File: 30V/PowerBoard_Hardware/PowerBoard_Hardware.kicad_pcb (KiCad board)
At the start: 2 copper layers, 145.4 x 114.3 mm, 114 parts, among them Q1 Q_NMOS_DGS, Q2 Q_NMOS_DGS, Q3 Q_NMOS_DGS, Q4 Q_NMOS_DGS, Q5 Q_NMOS_DGS, Q6 Q_NMOS_DGS, Q7 Q_NMOS_DGS, U1 LT1910, U10 LT1910, U11 LT1910, U12 ACS722xLCTR-40AU, U13 ACS722xLCTR-40AU, U14 ACS722xLCTR-40AU, U15 OKI, U16 OKI, U2 LT1910, U3 LT1910, U4 LT1910, U5 ACS722xLCTR-40AU, U6 ACS722xLCTR-40AU, U7 ACS722xLCTR-40AU, U8 ACS722xLCTR-40AU, U9 LT1910

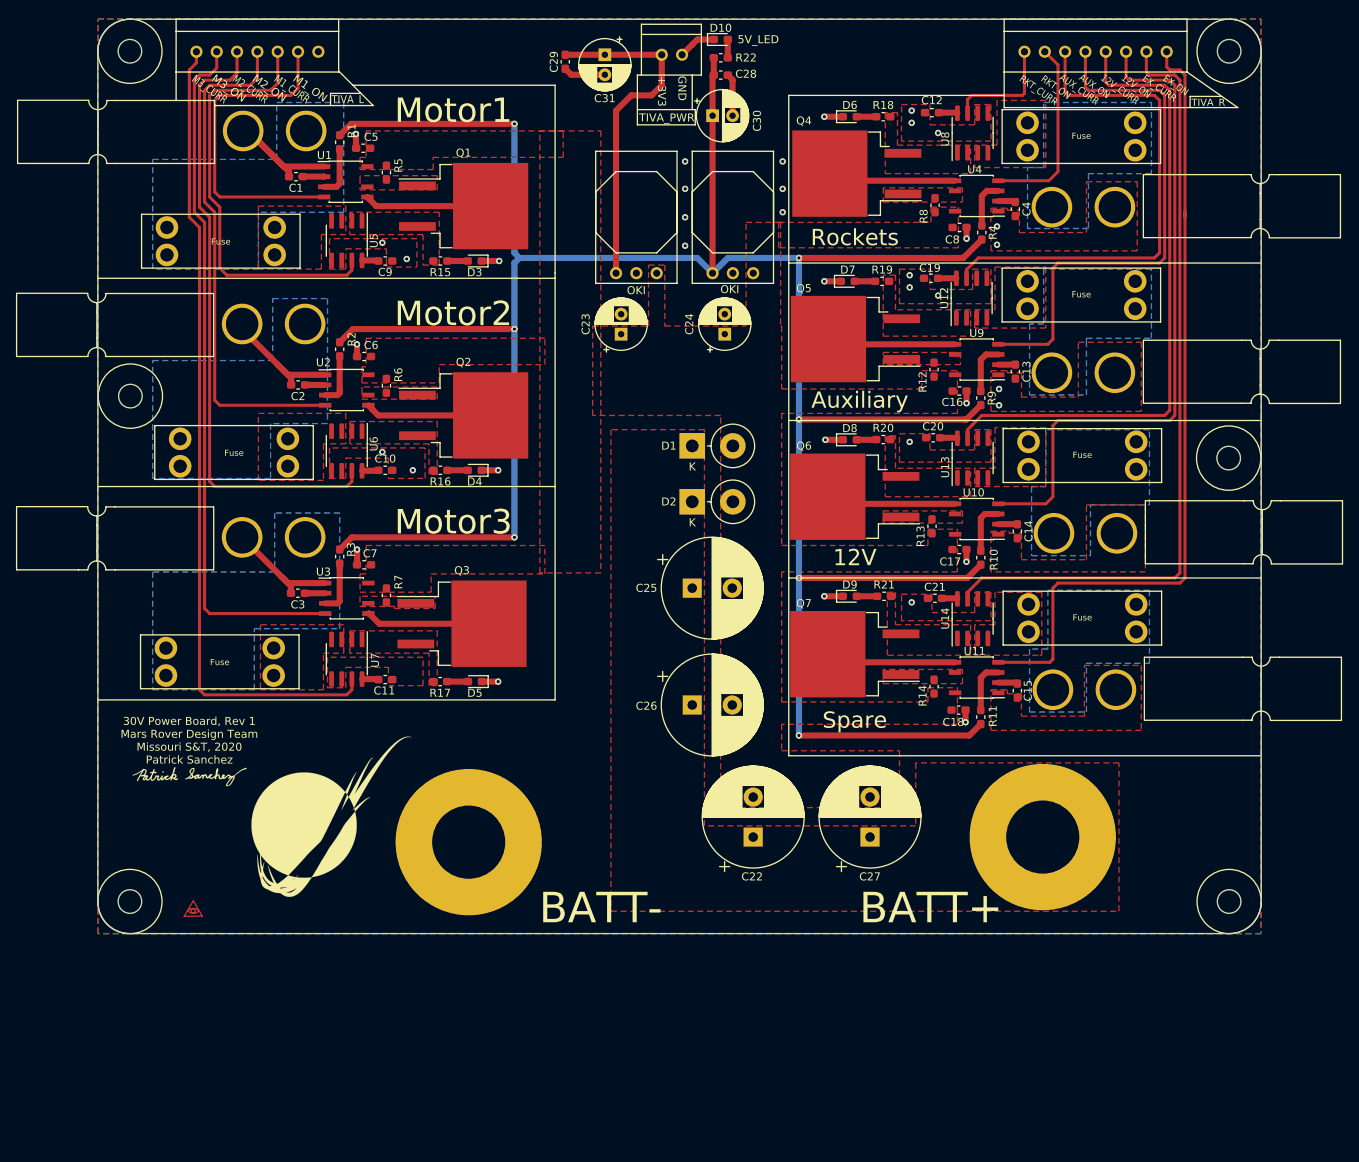
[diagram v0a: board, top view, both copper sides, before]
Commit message: Overwriting for proper file structure
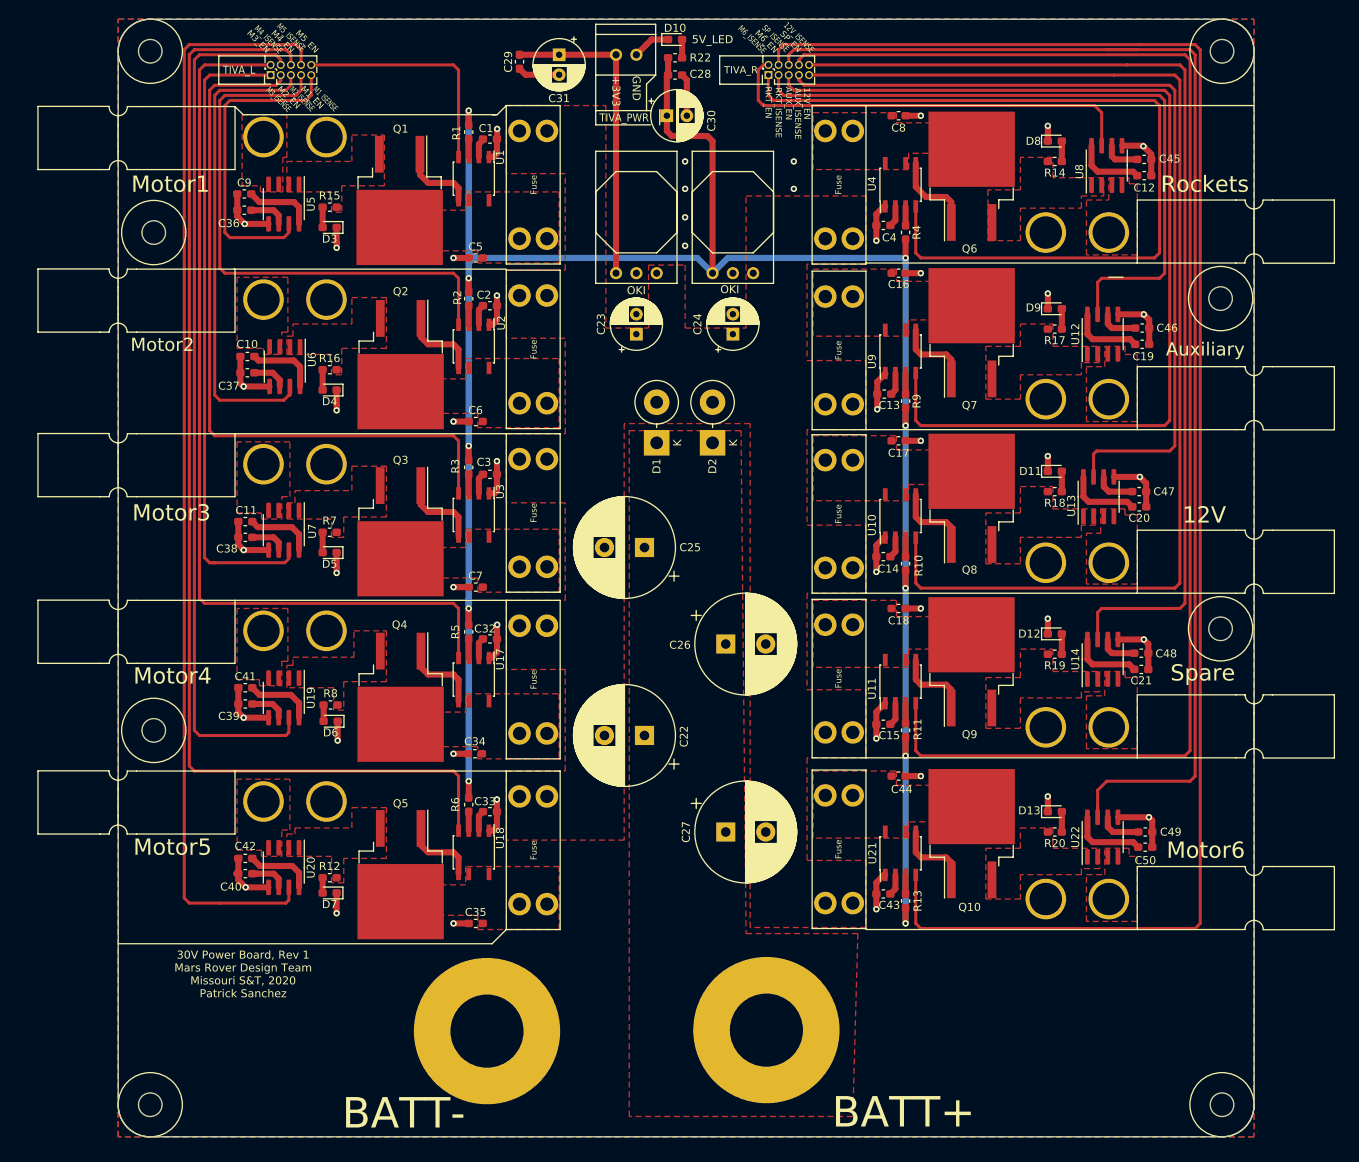
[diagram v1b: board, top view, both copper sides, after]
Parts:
- removed G***: LOGO, MRDT_Silkscreens:2_Nothing_3mm_Cu
- removed G***: LOGO, MRDT_Silkscreens:0_MRDT_Logo_20mm
- removed G***: LOGO, MRDT_Silkscreens:z_sig_Patrick_Sanchez_15mmx5mm
- removed R21: 1.5k, Resistor_SMD:R_0603_1608Metric_Pad1.05x0.95mm_HandSolder
- removed the REF** at (98.0, 77.6)
- removed the REF** at (235.3, 85.3)
- removed the REF** at (94.0, 144.8)
- removed the REF** at (239.4, 144.8)
- removed the REF** at (239.4, 30.5)
- removed the REF** at (94.0, 30.5)
- added C32: 0.1 uF, Capacitor_SMD:C_0603_1608Metric_Pad1.05x0.95mm_HandSolder, F.Cu at (143.0, 108.0)
- added C33: 0.1 uF, Capacitor_SMD:C_0603_1608Metric_Pad1.05x0.95mm_HandSolder, F.Cu at (143.0, 129.5)
- added C34: 10uF 50V, Capacitor_SMD:C_0603_1608Metric_Pad1.05x0.95mm_HandSolder, F.Cu at (141.1, 122.3)
- added C35: 10uF 50V, Capacitor_SMD:C_0603_1608Metric_Pad1.05x0.95mm_HandSolder, F.Cu at (141.2, 143.5)
- added C36: 1nF, Capacitor_SMD:C_0603_1608Metric_Pad1.05x0.95mm_HandSolder, F.Cu at (112.3, 54.4)
- added C37: 1nF, Capacitor_SMD:C_0603_1608Metric_Pad1.05x0.95mm_HandSolder, F.Cu at (112.7, 74.7)
- added C38: 1nF, Capacitor_SMD:C_0603_1608Metric_Pad1.05x0.95mm_HandSolder, F.Cu at (112.4, 95.2)
- added C39: 1nF, Capacitor_SMD:C_0603_1608Metric_Pad1.05x0.95mm_HandSolder, F.Cu at (112.4, 116.1)
- added C40: 1nF, Capacitor_SMD:C_0603_1608Metric_Pad1.05x0.95mm_HandSolder, F.Cu at (112.4, 137.3)
- added C41: 0.1 uF, Capacitor_SMD:C_0603_1608Metric_Pad1.05x0.95mm_HandSolder, F.Cu at (112.4, 114.0)
- added C42: 0.1 uF, Capacitor_SMD:C_0603_1608Metric_Pad1.05x0.95mm_HandSolder, F.Cu at (112.4, 135.4)
- added C43: 0.1 uF, Capacitor_SMD:C_0603_1608Metric_Pad1.05x0.95mm_HandSolder, F.Cu at (192.2, 139.8)
- added C44: 10uF 50V, Capacitor_SMD:C_0603_1608Metric_Pad1.05x0.95mm_HandSolder, F.Cu at (194.1, 125.1)
- added C45: 1nF, Capacitor_SMD:C_0603_1608Metric_Pad1.05x0.95mm_HandSolder, F.Cu at (224.8, 48.0)
- added C46: 1nF, Capacitor_SMD:C_0603_1608Metric_Pad1.05x0.95mm_HandSolder, F.Cu at (224.5, 69.1)
- added C47: 1nF, Capacitor_SMD:C_0603_1608Metric_Pad1.05x0.95mm_HandSolder, F.Cu at (224.1, 89.5)
- added C48: 1nF, Capacitor_SMD:C_0603_1608Metric_Pad1.05x0.95mm_HandSolder, F.Cu at (224.4, 109.7)
- added C49: 1nF, Capacitor_SMD:C_0603_1608Metric_Pad1.05x0.95mm_HandSolder, F.Cu at (224.9, 132.1)
- added C50: 0.1 uF, Capacitor_SMD:C_0603_1608Metric_Pad1.05x0.95mm_HandSolder, F.Cu at (224.9, 134.0)
- added Conn10: AndersonPP, MRDT_Connectors:Anderson_2_Horizontal_Stacked, F.Cu at (220.3, 140.5)
- added Conn6: AndersonPP, MRDT_Connectors:Anderson_2_Horizontal_Stacked, F.Cu at (220.3, 57.1)
- added Conn7: AndersonPP, MRDT_Connectors:Anderson_2_Horizontal_Stacked, F.Cu at (220.3, 78.0)
- added D11: GRN, LED_SMD:LED_0603_1608Metric_Pad1.05x0.95mm_HandSolder, F.Cu at (213.6, 87.0)
- added D12: ORG, LED_SMD:LED_0603_1608Metric_Pad1.05x0.95mm_HandSolder, F.Cu at (213.6, 107.3)
- added D13: ORG, LED_SMD:LED_0603_1608Metric_Pad1.05x0.95mm_HandSolder, F.Cu at (213.6, 129.5)
- added F10: Fuse, MRDT_Passives:ATC_Fuse_Block, F.Cu at (190.0, 144.1)
- added F8: Fuse, MRDT_Passives:ATC_Fuse_Block, F.Cu at (145.0, 103.1)
- added F9: Fuse, MRDT_Passives:ATC_Fuse_Block, F.Cu at (145.0, 124.5)
- added Q10: Q_NMOS_GDS, Package_TO_SOT_SMD:TO-263-2, F.Cu at (203.2, 132.3)
- added Q8: Q_NMOS_GDS, Package_TO_SOT_SMD:TO-263-2, F.Cu at (203.2, 90.4)
- added Q9: Q_NMOS_GDS, Package_TO_SOT_SMD:TO-263-2, F.Cu at (203.2, 110.8)
- added REF**: 4_40_Hole, MRDT_Drill_Holes:4_40_Hole_Corner, F.Cu at (96.5, 170.2)
- added REF**: 4_40_Hole, MRDT_Drill_Holes:4_40_Hole_Corner, F.Cu at (238.5, 170.2)
- added REF**: 4_40_Hole, MRDT_Drill_Holes:4_40_Hole_Corner, F.Cu at (238.5, 30.5)
- added REF**: 4_40_Hole, MRDT_Drill_Holes:4_40_Hole, F.Cu at (101.0, 119.4)
- added REF**: 4_40_Hole, MRDT_Drill_Holes:4_40_Hole, F.Cu at (234.3, 106.7)
- added REF**: 4_40_Hole, MRDT_Drill_Holes:4_40_Hole, F.Cu at (234.3, 65.4)
- added REF**: 4_40_Hole, MRDT_Drill_Holes:4_40_Hole, F.Cu at (101.0, 57.1)
- added REF**: 4_40_Hole, MRDT_Drill_Holes:4_40_Hole_Corner, F.Cu at (96.5, 30.5)
- added U17: LT1910, Package_SO:SOIC-8-N7_3.9x4.9mm_P1.27mm, F.Cu at (141.0, 113.0)
- added U18: LT1910, Package_SO:SOIC-8-N7_3.9x4.9mm_P1.27mm, F.Cu at (141.0, 134.6)
- added U19: ACS722xLCTR-40AU, Package_SO:SOIC-8_3.9x4.9mm_P1.27mm, F.Cu at (117.2, 115.3)
- added U20: ACS722xLCTR-40AU, Package_SO:SOIC-8_3.9x4.9mm_P1.27mm, F.Cu at (117.2, 136.5)
- added U21: LT1910, Package_SO:SOIC-8-N7_3.9x4.9mm_P1.27mm, F.Cu at (194.3, 134.7)
- added U22: ACS722xLCTR-40AU, Package_SO:SOIC-8_3.9x4.9mm_P1.27mm, F.Cu at (219.6, 132.7)
- C16, C17, C18, C5, C6, C7, C8: value 10uF -> 10uF 50V
- ConnTIVA_L1: value Molex_SL_07 -> PH_2x05; footprint MRDT_Connectors:MOLEX_SL_07_Vertical -> Connector_PinHeader_1.27mm:PinHeader_2x05_P1.27mm_Vertical
- ConnTIVA_PWR1: value Molex_SL_04 -> Molex_SL_02
- ConnTIVA_R1: value Molex_SL_08 -> PH_2x05; footprint MRDT_Connectors:MOLEX_SL_08_Vertical -> Connector_PinHeader_1.27mm:PinHeader_2x05_P1.27mm_Vertical
- D10: value LED_+5V -> GRN
- D3, D4, D5, D6, D7: value LED -> ORG
- D8, D9: value LED -> BLU
- Q1, Q2, Q3, Q4, Q5, Q6, Q7: value Q_NMOS_DGS -> Q_NMOS_GDS
- R12, R14, R7, R8: value 0.01 -> 2.5k
- R13, R5, R6: value 0.01 -> 5.1k
- R15, R16, R17, R18, R19, R20: value 1.5k -> 2.5k
- moved Conn5 119.2 mm to (114.7, 128.3), turned to 0 degrees
- moved Conn4 118.9 mm to (114.7, 106.9), turned to 0 degrees
- moved D7 100.2 mm to (123.0, 139.7), turned to 180 degrees
- moved D6 99.6 mm to (123.1, 118.2), turned to 180 degrees
- moved R12 98.7 mm to (123.0, 137.8), turned to 0 degrees
- moved R8 98.0 mm to (123.1, 116.2), turned to 0 degrees
- moved R17 88.6 mm to (213.6, 69.2)
- moved Q5 87.8 mm to (131.8, 137.4), turned to 270 degrees
- moved Q4 86.8 mm to (131.8, 115.2), turned to 270 degrees
- moved R14 67.4 mm to (213.6, 48.3), turned to 180 degrees
- moved R5 58.3 mm to (140.3, 107.1)
- moved R20 53.5 mm to (213.6, 132.1), turned to 180 degrees
- moved R6 53.4 mm to (140.3, 128.7)
- moved R18 51.5 mm to (213.6, 89.5), turned to 180 degrees
- moved R19 51.4 mm to (213.6, 109.9), turned to 180 degrees
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- renumbered Conn6 to Conn8, Conn7 to Conn9
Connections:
- net AUX_CURR renamed AUX_ISENSE
- net EX_ON renamed SP_EN
- net M3_CURR renamed M3_ISENSE
- net Net-(Q1-Pad3) renamed M1_LED
- net Net-(Q2-Pad3) renamed M2_LED
- C16 pad 1: PVDD -> Net-(C16-Pad1)
- C17 pad 1: PVDD -> Net-(C17-Pad1)
- C18 pad 1: PVDD -> Net-(C18-Pad1)
- C5 pad 1: PVDD -> Net-(C5-Pad1)
- C6 pad 1: PVDD -> Net-(C6-Pad1)
- C7 pad 1: PVDD -> Net-(C7-Pad1)
- C8 pad 1: PVDD -> Net-(C8-Pad1)
- Conn1 pad 1: GND -> Net-(Conn1-Pad1)
- Conn1 pad 4: Net-(Conn1-Pad4) -> GND
- Conn2 pad 1: GND -> Net-(Conn2-Pad1)
- Conn2 pad 4: Net-(Conn2-Pad4) -> GND
- Conn3 pad 1: GND -> Net-(Conn3-Pad1)
- Conn3 pad 4: Net-(Conn3-Pad4) -> GND
- Conn4 pad 1: GND -> Net-(Conn4-Pad1)
- Conn4 pad 4: (no net) -> GND
- Conn5 pad 1: GND -> Net-(Conn5-Pad1)
- Conn5 pad 4: Net-(Conn5-Pad4) -> GND
- Conn8 pad 1: GND -> Net-(Conn8-Pad1)
- Conn8 pad 4: Net-(Conn6-Pad4) -> GND
- Conn9 pad 1: GND -> Net-(Conn9-Pad1)
- Conn9 pad 4: Net-(Conn7-Pad4) -> GND
- ConnTIVA_L1 pad 2: M3_ON -> M4_EN
- ConnTIVA_L1 pad 3: M2_CURR -> M3_EN
- ConnTIVA_L1 pad 4: M2_ON -> M4_ISENSE
- ConnTIVA_L1 pad 5: M1_CURR -> M2_ISENSE
- ConnTIVA_L1 pad 6: M1_ON -> M5_EN
- ConnTIVA_L1 pad 7: Net-(ConnTIVA_L1-Pad7) -> M2_EN
- ConnTIVA_R1 pad 1: RKT_CURR -> RKT_EN
- ConnTIVA_R1 pad 2: RKT_ON -> RKT_ISENSE
- ConnTIVA_R1 pad 4: AUX_ON -> M6_EN
- ConnTIVA_R1 pad 5: 12V_CURR -> AUX_EN
- ConnTIVA_R1 pad 6: 12V_ON -> M6_ISENSE
- ConnTIVA_R1 pad 7: EX_CURR -> 12V_ISENSE
- F1 pad 1: Net-(F1-Pad1) -> PVDD
- F1 pad 2: Net-(Conn1-Pad4) -> Net-(C5-Pad1)
- F2 pad 1: Net-(F2-Pad1) -> PVDD
- F2 pad 2: Net-(Conn2-Pad4) -> Net-(C6-Pad1)
- F3 pad 1: Net-(F3-Pad1) -> PVDD
- F3 pad 2: Net-(Conn3-Pad4) -> Net-(C7-Pad1)
- F4 pad 1: Net-(F4-Pad1) -> PVDD
- F4 pad 2: Net-(Conn4-Pad1) -> Net-(C8-Pad1)
- F5 pad 1: Net-(F5-Pad1) -> PVDD
- F5 pad 2: Net-(Conn5-Pad4) -> Net-(C16-Pad1)
- F6 pad 1: Net-(F6-Pad1) -> PVDD
- F6 pad 2: Net-(Conn6-Pad4) -> Net-(C17-Pad1)
- F7 pad 1: Net-(F7-Pad1) -> PVDD
- F7 pad 2: Net-(Conn7-Pad4) -> Net-(C18-Pad1)
- Q1 pad 2: Net-(Q1-Pad2) -> Net-(C5-Pad1)
- Q2 pad 2: Net-(Q2-Pad2) -> Net-(C6-Pad1)
- Q3 pad 2: Net-(Q3-Pad2) -> Net-(C7-Pad1)
- Q3 pad 3: Net-(Q3-Pad3) -> M3_LED
- Q4 pad 2: Net-(Q4-Pad2) -> Net-(C34-Pad1)
- Q4 pad 3: Net-(Q4-Pad3) -> M4_LED
- Q5 pad 2: Net-(Q5-Pad2) -> Net-(C35-Pad1)
- Q5 pad 3: Net-(Q5-Pad3) -> M5_LED
- Q6 pad 2: Net-(Q6-Pad2) -> Net-(C8-Pad1)
- Q6 pad 3: Net-(Q6-Pad3) -> RKT_LED
- Q7 pad 2: Net-(Q7-Pad2) -> Net-(C16-Pad1)
- Q7 pad 3: Net-(Q7-Pad3) -> AUX_LED
- R12 pad 1: PVDD -> Net-(D7-Pad2)
- R12 pad 2: Net-(Q5-Pad1) -> M5_LED
- R13 pad 1: PVDD -> +5V
- R13 pad 2: Net-(Q6-Pad1) -> Net-(R13-Pad2)
- R14 pad 1: PVDD -> Net-(D8-Pad2)
- R14 pad 2: Net-(Q7-Pad1) -> RKT_LED
- R17 pad 1: Net-(D5-Pad2) -> Net-(D9-Pad2)
- R17 pad 2: Net-(Q3-Pad3) -> AUX_LED
- R18 pad 1: Net-(D6-Pad2) -> Net-(D11-Pad2)
- R18 pad 2: Net-(Q4-Pad3) -> 12V_LED
- R19 pad 1: Net-(D7-Pad2) -> Net-(D12-Pad2)
- R19 pad 2: Net-(Q5-Pad3) -> SP_LED
- R20 pad 1: Net-(D8-Pad2) -> Net-(D13-Pad2)
- R20 pad 2: Net-(Q6-Pad3) -> M6_LED
- R5 pad 1: PVDD -> +5V
- R5 pad 2: Net-(Q1-Pad1) -> Net-(R5-Pad2)
- R6 pad 1: PVDD -> +5V
- R6 pad 2: Net-(Q2-Pad1) -> Net-(R6-Pad2)
- R7 pad 1: PVDD -> Net-(D5-Pad2)
- R7 pad 2: Net-(Q3-Pad1) -> M3_LED
- R8 pad 1: PVDD -> Net-(D6-Pad2)
- R8 pad 2: Net-(Q4-Pad1) -> M4_LED
- U1 pad 4: M1_ON -> M1_EN
- U1 pad 5: Net-(Q1-Pad2) -> Net-(Q1-Pad1)
- U1 pad 6: Net-(Q1-Pad1) -> Net-(C5-Pad1)
- U1 pad 8: PVDD -> Net-(C5-Pad1)
- U10 pad 4: 12V_ON -> 12V_EN
- U10 pad 5: Net-(Q6-Pad2) -> Net-(Q8-Pad1)
- U10 pad 6: Net-(Q6-Pad1) -> Net-(C17-Pad1)
- U10 pad 8: PVDD -> Net-(C17-Pad1)
- U11 pad 5: Net-(Q7-Pad2) -> Net-(Q9-Pad1)
- U11 pad 6: Net-(Q7-Pad1) -> Net-(C18-Pad1)
- U11 pad 8: PVDD -> Net-(C18-Pad1)
- U12 pad 1: Net-(Q5-Pad3) -> AUX_LED
- U12 pad 2: Net-(Q5-Pad3) -> AUX_LED
- U12 pad 3: Net-(F5-Pad1) -> Net-(Conn7-Pad1)
- U12 pad 4: Net-(F5-Pad1) -> Net-(Conn7-Pad1)
- U12 pad 6: GND -> Net-(C46-Pad1)
- U13 pad 1: Net-(Q6-Pad3) -> 12V_LED
- U13 pad 2: Net-(Q6-Pad3) -> 12V_LED
- U13 pad 3: Net-(F6-Pad1) -> Net-(Conn8-Pad1)
- U13 pad 4: Net-(F6-Pad1) -> Net-(Conn8-Pad1)
- U13 pad 6: GND -> Net-(C47-Pad1)
- U13 pad 7: 12V_CURR -> 12V_ISENSE
- U14 pad 1: Net-(Q7-Pad3) -> SP_LED
- U14 pad 2: Net-(Q7-Pad3) -> SP_LED
- U14 pad 3: Net-(F7-Pad1) -> Net-(Conn9-Pad1)
- U14 pad 4: Net-(F7-Pad1) -> Net-(Conn9-Pad1)
- U14 pad 6: GND -> Net-(C48-Pad1)
- U14 pad 7: EX_CURR -> SP_ISENSE
- U2 pad 4: M2_ON -> M2_EN
- U2 pad 5: Net-(Q2-Pad2) -> Net-(Q2-Pad1)
- U2 pad 6: Net-(Q2-Pad1) -> Net-(C6-Pad1)
- U2 pad 8: PVDD -> Net-(C6-Pad1)
- U3 pad 4: M3_ON -> M3_EN
- U3 pad 5: Net-(Q3-Pad2) -> Net-(Q3-Pad1)
- U3 pad 6: Net-(Q3-Pad1) -> Net-(C7-Pad1)
- U3 pad 8: PVDD -> Net-(C7-Pad1)
- U4 pad 4: RKT_ON -> RKT_EN
- U4 pad 5: Net-(Q4-Pad2) -> Net-(Q6-Pad1)
- U4 pad 6: Net-(Q4-Pad1) -> Net-(C8-Pad1)
- U4 pad 8: PVDD -> Net-(C8-Pad1)
- U5 pad 3: Net-(F1-Pad1) -> Net-(Conn1-Pad1)
- U5 pad 4: Net-(F1-Pad1) -> Net-(Conn1-Pad1)
- U5 pad 6: GND -> Net-(C36-Pad1)
- U5 pad 7: M1_CURR -> M1_ISENSE
- U6 pad 3: Net-(F2-Pad1) -> Net-(Conn2-Pad1)
- U6 pad 4: Net-(F2-Pad1) -> Net-(Conn2-Pad1)
- U6 pad 6: GND -> Net-(C37-Pad1)
- U6 pad 7: M2_CURR -> M2_ISENSE
- U7 pad 1: Net-(Q3-Pad3) -> M3_LED
- U7 pad 2: Net-(Q3-Pad3) -> M3_LED
- U7 pad 3: Net-(F3-Pad1) -> Net-(Conn3-Pad1)
- U7 pad 4: Net-(F3-Pad1) -> Net-(Conn3-Pad1)
- U7 pad 6: GND -> Net-(C38-Pad1)
- U8 pad 1: Net-(Q4-Pad3) -> RKT_LED
- U8 pad 2: Net-(Q4-Pad3) -> RKT_LED
- U8 pad 3: Net-(F4-Pad1) -> Net-(Conn6-Pad1)
- U8 pad 4: Net-(F4-Pad1) -> Net-(Conn6-Pad1)
- U8 pad 6: GND -> Net-(C45-Pad1)
- U8 pad 7: RKT_CURR -> RKT_ISENSE
- U9 pad 4: AUX_ON -> AUX_EN
- U9 pad 5: Net-(Q5-Pad2) -> Net-(Q7-Pad1)
- U9 pad 6: Net-(Q5-Pad1) -> Net-(C16-Pad1)
- U9 pad 8: PVDD -> Net-(C16-Pad1)
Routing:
- net M6_EN: track 0.00 -> 206.9 mm
- net M6_ISENSE: track 0.00 -> 164.2 mm
- net 12V_EN: track 0.00 -> 148.7 mm
- net M5_EN: track 0.00 -> 144.4 mm
- net M5_ISENSE: track 0.00 -> 138.2 mm
- net SP_ISENSE: track 0.00 -> 128.7 mm
- net AUX_EN: track 0.00 -> 128.3 mm
- net M4_EN: track 0.00 -> 114.3 mm
- net M4_ISENSE: track 0.00 -> 109.9 mm
- net RKT_EN: track 0.00 -> 107.2 mm
- net 12V_ISENSE: track 0.00 -> 106.0 mm
- net EX_CURR: track 97.4 -> 0.00 mm
- net M3_EN: track 0.00 -> 90.9 mm
- net M3_ON: track 87.4 -> 0.00 mm
- net 12V_ON: track 82.8 -> 0.00 mm
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- added copper zone on F.Cu, net 12V_LED
- added copper zone on F.Cu, net AUX_LED
- added copper zone on F.Cu, net M3_LED
- added copper zone on F.Cu, net M4_LED
- added copper zone on F.Cu, net M5_LED
- added copper zone on F.Cu, net M6_LED
- added copper zone on F.Cu, net Net-(C16-Pad1)
- added copper zone on F.Cu, net Net-(C17-Pad1)
- added copper zone on F.Cu, net Net-(C18-Pad1)
- added copper zone on F.Cu, net Net-(C34-Pad1)
- added copper zone on F.Cu, net Net-(C35-Pad1)
- added copper zone on F.Cu, net Net-(C44-Pad1)
- added copper zone on F.Cu, net Net-(C5-Pad1)
- added copper zone on F.Cu, net Net-(C6-Pad1)
- added copper zone on F.Cu, net Net-(C7-Pad1)
- added copper zone on F.Cu, net Net-(C8-Pad1)
- added copper zone on F.Cu, net Net-(Conn1-Pad1)
- added copper zone on F.Cu, net Net-(Conn10-Pad1)
- added copper zone on F.Cu, net Net-(Conn2-Pad1)
- added copper zone on F.Cu, net Net-(Conn3-Pad1)
- added copper zone on F.Cu, net Net-(Conn4-Pad1)
- added copper zone on F.Cu, net Net-(Conn5-Pad1)
- added copper zone on F.Cu, net Net-(Conn6-Pad1)
- added copper zone on F.Cu, net Net-(Conn7-Pad1)
- added copper zone on F.Cu, net Net-(Conn8-Pad1)
- added copper zone on F.Cu, net Net-(Conn9-Pad1)
- added copper zone on F.Cu, net RKT_LED
- added copper zone on F.Cu, net SP_LED
- removed copper zone on B.Cu, net Net-(Conn1-Pad4)
- removed copper zone on B.Cu, net Net-(Conn2-Pad4)
- removed copper zone on B.Cu, net Net-(Conn3-Pad4)
- removed copper zone on B.Cu, net Net-(Conn4-Pad1)
- removed copper zone on B.Cu, net Net-(Conn5-Pad4)
- removed copper zone on B.Cu, net Net-(Conn6-Pad4)
- removed copper zone on B.Cu, net Net-(Conn7-Pad4)
- removed copper zone on F.Cu, net Net-(F1-Pad1)
- removed copper zone on F.Cu, net Net-(F2-Pad1)
- removed copper zone on F.Cu, net Net-(F3-Pad1)
- removed copper zone on F.Cu, net Net-(F4-Pad1)
- removed copper zone on F.Cu, net Net-(F5-Pad1)
- removed copper zone on F.Cu, net Net-(F6-Pad1)
- removed copper zone on F.Cu, net Net-(F7-Pad1)
- removed copper zone on F.Cu, net Net-(Q1-Pad1)
- removed copper zone on F.Cu, net Net-(Q2-Pad1)
- removed copper zone on F.Cu, net Net-(Q3-Pad1)
- removed copper zone on F.Cu, net Net-(Q3-Pad3)
- removed copper zone on F.Cu, net Net-(Q4-Pad1)
- removed copper zone on F.Cu, net Net-(Q4-Pad3)
- removed copper zone on F.Cu, net Net-(Q5-Pad1)
- removed copper zone on F.Cu, net Net-(Q5-Pad3)
- removed copper zone on F.Cu, net Net-(Q6-Pad1)
- removed copper zone on F.Cu, net Net-(Q6-Pad3)
- removed copper zone on F.Cu, net Net-(Q7-Pad1)
- removed copper zone on F.Cu, net Net-(Q7-Pad3)
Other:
- board size 145.4 x 114.3 mm -> 142 x 139.7 mm
- board text added: "12V_EN"
- board text added: "12V_ISENSE"
- board text added: "AUX_EN"
- board text added: "AUX_ISENSE"
- board text added: "M1_EN"
- board text added: "M1_ISENSE"
- board text added: "M2_EN"
- board text added: "M2_ISENSE"
- board text added: "M3_EN"
- board text added: "M3_ISENSE"
- board text added: "M4_EN"
- board text added: "M4_ISENSE"
- board text added: "M5_EN"
- board text added: "M5_ISENSE"
- board text added: "M6_EN"
- board text added: "M6_ISENSE"
- board text added: "Motor4"
- board text added: "Motor5"
- board text added: "Motor6"
- board text added: "RKT_EN"
- board text added: "RKT_ISENSE"
- board text added: "SP_EN"
- board text added: "SP_ISENSE"
- board text removed: "12V_CURR"
- board text removed: "12V_ON"
- board text removed: "AUX_CURR"
- board text removed: "AUX_ON"
- board text removed: "EX_CURR"
- board text removed: "EX_ON"
- board text removed: "M1_CURR"
- board text removed: "M1_ON"
- board text removed: "M2_CURR"
- board text removed: "M2_ON"
- board text removed: "M3_CURR"
- board text removed: "M3_ON"
- board text removed: "RKT_CURR"
- board text removed: "RKT_ON"

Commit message: Added BOM, changed a capacitor to larger type for 50V, changed some labels
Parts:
- C1, C12, C13, C14, C15, C19, C2, C20, C21, C3, C32, C33, C4, C41, C42, C43, C50: value 0.1 uF -> 0.1uF
- C16, C17, C18, C34, C35, C44, C5, C6, C7, C8: footprint Capacitor_SMD:C_0603_1608Metric_Pad1.05x0.95mm_HandSolder -> Capacitor_SMD:C_1206_3216Metric_Pad1.42x1.75mm_HandSolder
- U15: value OKI -> OKI_5V
- U16: value OKI -> OKI_3V3
- moved C8 0.88 mm to (193.5, 43.2)
- moved C34 0.71 mm to (141.8, 122.3)
- moved C16 0.61 mm to (193.5, 62.2)
- moved C17 0.61 mm to (193.5, 83.2)
- moved C18 0.61 mm to (193.5, 104.1)
- moved C35 0.61 mm to (141.8, 143.5)
- moved C44 0.61 mm to (193.5, 125.1)
- moved C5 0.61 mm to (141.8, 60.3)
- moved C6 0.61 mm to (141.8, 80.8)
- moved C7 0.61 mm to (141.8, 101.5)

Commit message: Ready for PRR
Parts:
- added G***: LOGO, Custom_Footprints:z_sig_Patrick_Sanchez_15mmx5mm, F.Cu at (112.3, 154.7)

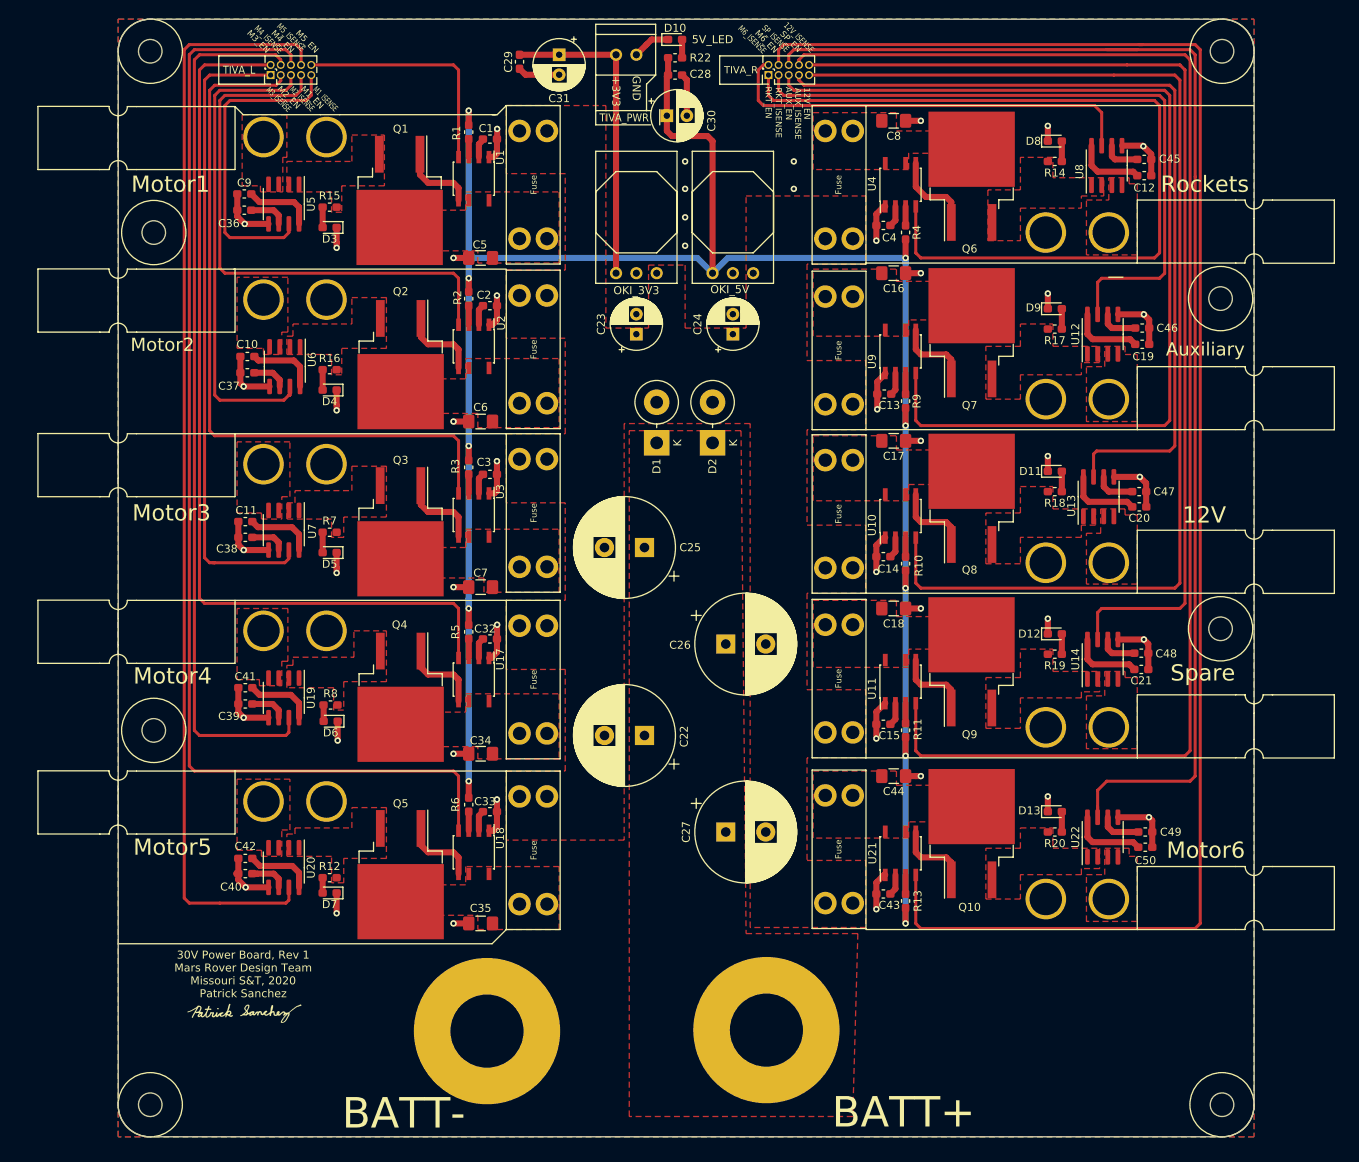
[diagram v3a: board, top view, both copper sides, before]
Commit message: redid PVDD
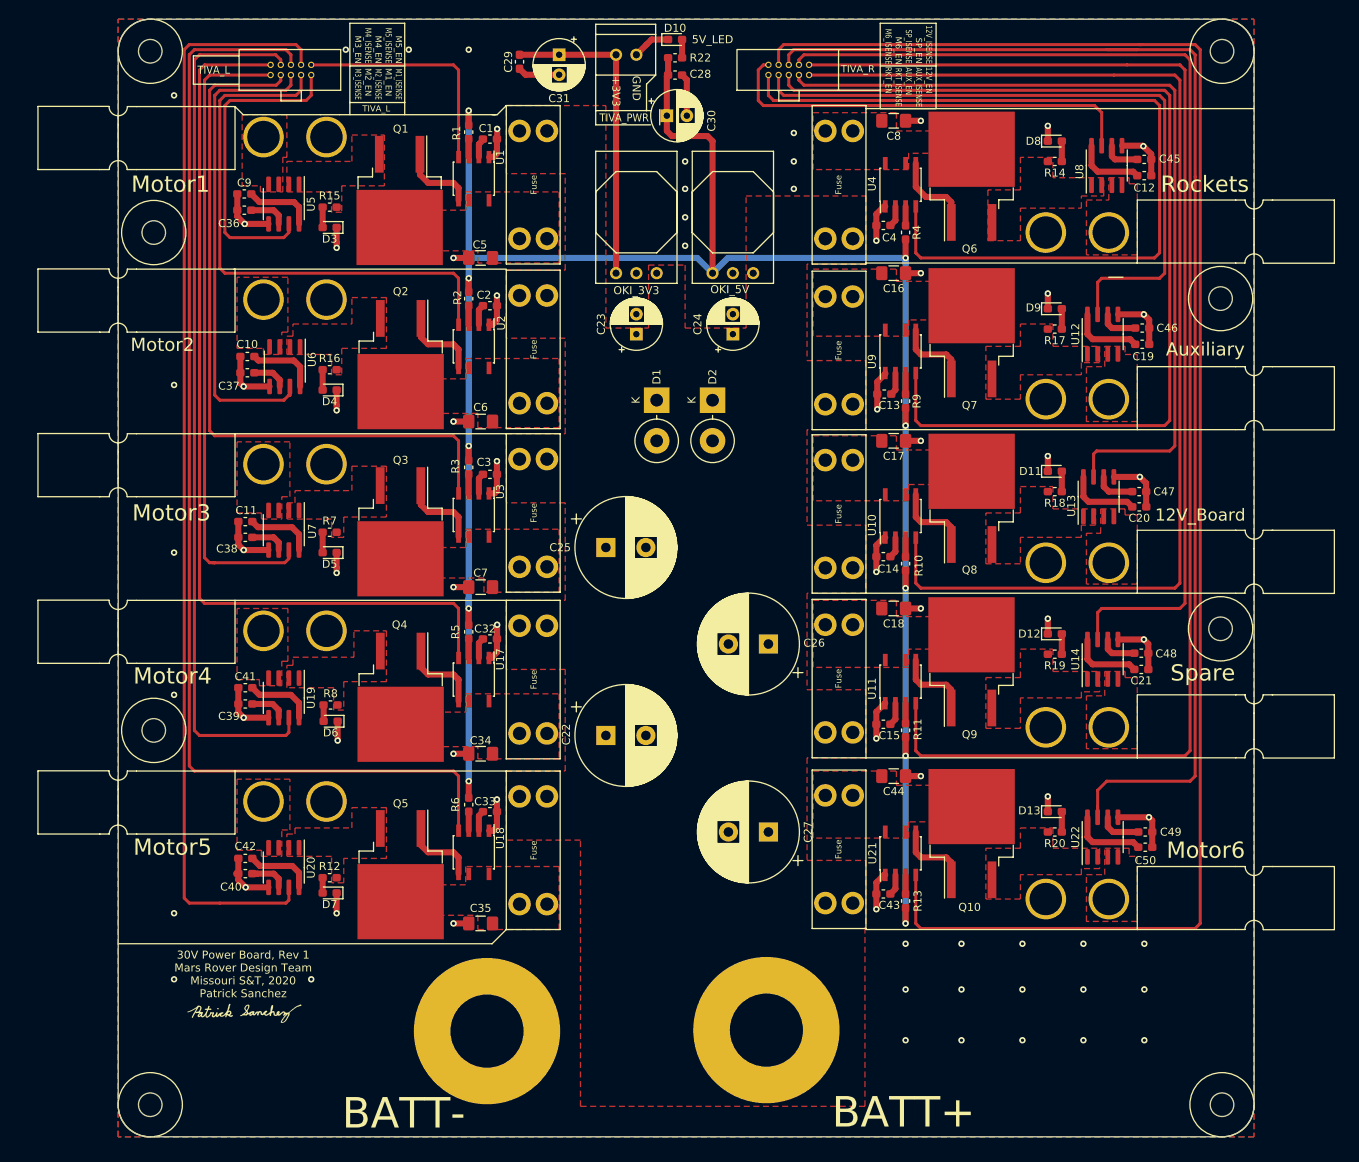
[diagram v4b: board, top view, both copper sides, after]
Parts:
- ConnTIVA_L1, ConnTIVA_R1: footprint Connector_PinHeader_1.27mm:PinHeader_2x05_P1.27mm_Vertical -> MRDT_Connectors:JTAG_ARM_Connector_10_Pin
- moved C26 5.33 mm to (177.8, 108.6), turned to 180 degrees
- moved C27 5.33 mm to (177.8, 132.1), turned to 180 degrees
- moved D1 5.33 mm to (163.8, 78.1), turned to 270 degrees
- moved D2 5.33 mm to (170.8, 78.1), turned to 270 degrees
- moved C22 4.83 mm to (157.5, 120.0), turned to 0 degrees
- moved C25 4.83 mm to (157.5, 96.5), turned to 0 degrees
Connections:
- C22 pad 1: Net-(C22-Pad1) -> PVDD
- C22 pad 2: PVDD -> GND
- C25 pad 1: Net-(C22-Pad1) -> PVDD
- C25 pad 2: PVDD -> GND
- C26 pad 1: Net-(C22-Pad1) -> PVDD
- C26 pad 2: PVDD -> GND
- C27 pad 1: Net-(C22-Pad1) -> PVDD
- C27 pad 2: PVDD -> GND
- D1 pad 1: Net-(C22-Pad1) -> PVDD
- D1 pad 2: PVDD -> GND
- D2 pad 1: Net-(C22-Pad1) -> PVDD
- D2 pad 2: PVDD -> GND
- V1 pad 1: Net-(C22-Pad1) -> PVDD
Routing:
- net GND: vias 46 -> 72
- removed copper zone on F.Cu, net Net-(C22-Pad1)
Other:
- board text added: "12V_Board"
- board text removed: "12V"
